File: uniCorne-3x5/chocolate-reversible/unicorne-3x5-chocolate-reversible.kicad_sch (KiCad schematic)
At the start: 87 parts, among them J1 MJ-4PP-9, J2 Conn_01x05, J3 Conn_01x02, J3 Conn_01x03, SW1 SW_CHOC_HS, SW10 SW_CHOC_HS, SW11 SW_CHOC_HS, SW12 SW_CHOC_HS, SW13 SW_CHOC_HS, SW14 SW_CHOC_HS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

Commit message: amended chocolate 3x5
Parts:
- U1: footprint TB2086_MISC:ProMicro-ish-dn-rev-unrouted_3x5 -> TB2086_MISC:ProMicro-ish-dn-rev-unrouted_3x6
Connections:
- net BAT+: now also PSW1.1 (A); no longer PSW1.3 (C)

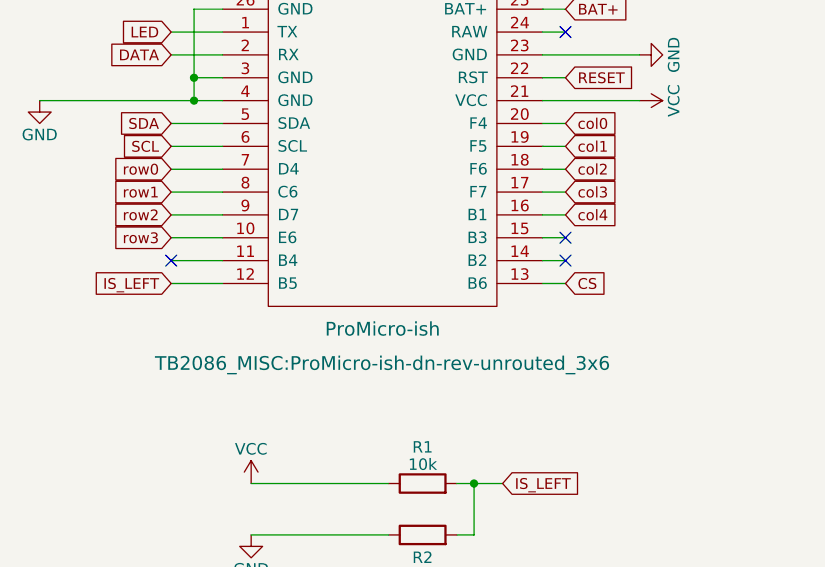
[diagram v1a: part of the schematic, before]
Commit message: fixed footprint for promicro-ish 3x6
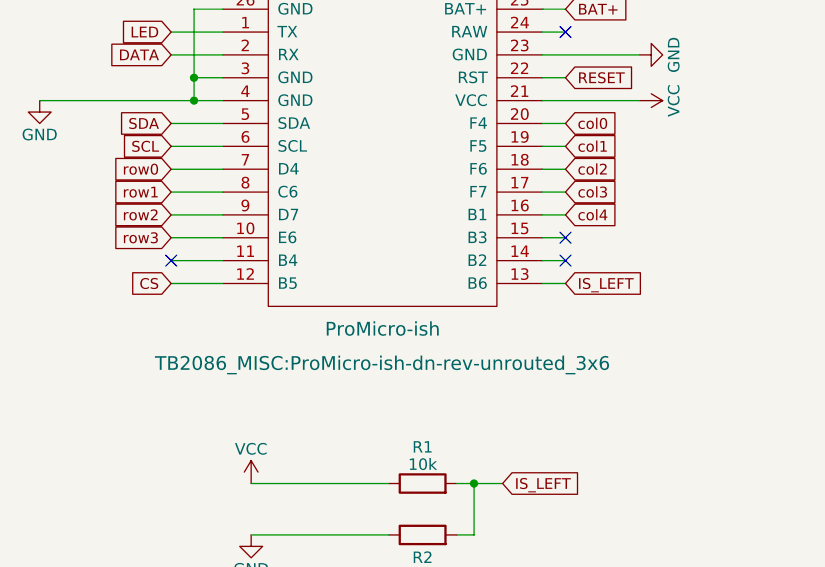
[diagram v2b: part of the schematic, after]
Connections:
- net CS: now also U1.12 (B5); no longer U1.13 (B6)
- net IS_LEFT: now also U1.13 (B6); no longer U1.12 (B5)
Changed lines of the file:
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@@
     )
   )
-  (global_label "CS" (shape input) (at 80.645 54.61 0) (fields_autoplaced)
+  (global_label "IS_LEFT" (shape input) (at 80.645 54.61 0) (fields_autoplaced)
     (effects (font (size 1.1938 1.1938)) (justify left))
-    (property "Intersheetrefs" "${INTERSHEET_REFS}" (at 85.7069 54.61 0)
+    (property "Intersheetrefs" "${INTERSHEET_REFS}" (at 89.9706 54.61 0)
       (effects (font (size 1.27 1.27)) (justify left) hide)
     )
@@
     )
   )
-  (global_label "IS_LEFT" (shape input) (at 36.83 54.61 180) (fields_autoplaced)
+  (global_label "CS" (shape input) (at 36.83 54.61 180) (fields_autoplaced)
     (effects (font (size 1.1938 1.1938)) (justify right))
-    (property "Intersheetrefs" "${INTERSHEET_REFS}" (at 27.5044 54.61 0)
+    (property "Intersheetrefs" "${INTERSHEET_REFS}" (at 31.7681 54.61 0)
       (effects (font (size 1.27 1.27)) (justify right) hide)
     )

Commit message: fixed 3x5
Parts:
- added JP10, JP11: (no value), TB2086_MISC:SolderJumper-2_P1.3mm_Open_TrianglePad1.0x1.2mm_rev, symbol Jumper:Jumper_2_Open
- U1: footprint TB2086_MISC:ProMicro-ish-dn-rev-unrouted_3x6 -> TB2086_MISC:ProMicro-ish-dn-rev-unrouted_3x5
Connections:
- net BAT+: now also U1.24 (RAW)
- net GND: now also JP11.2 (B); no longer U1.26 (GND)
- net SCL: now also JP10.1 (A); no longer J1.A
- new net: J1.A, JP10.2 (B)
- new net B-/D-: JP11.1 (A), U1.26 (B-/D-)
- no-connect marks 6 -> 5
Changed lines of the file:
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@@
   (junction (at 361.95 198.12) (diameter 0) (color 0 0 0 0)
   )
-  (junction (at 39.37 31.75) (diameter 0) (color 0 0 0 0)
-  )
   (junction (at 53.975 129.54) (diameter 0) (color 0 0 0 0)
   )
@@
   )
   (no_connect (at 36.83 52.07))
-  (no_connect (at 80.645 26.67))
   (no_connect (at 261.62 168.91))
   (no_connect (at 59.69 207.645))
@@
     (stroke (width 0) (type default))
   )
-  (wire (pts (xy 108.585 119.38) (xy 156.845 119.38))
+  (wire (pts (xy 108.585 119.38) (xy 117.475 119.38))
     (stroke (width 0) (type default))
   )
@@
     (stroke (width 0) (type default))
   )
-  (wire (pts (xy 39.37 24.13) (xy 39.37 31.75))
-    (stroke (width 0) (type default))
-  )
   (wire (pts (xy 257.81 95.885) (xy 254 95.885))
     (stroke (width 0) (type default))
@@
     (stroke (width 0) (type default))
   )
+  (wire (pts (xy 124.587 171.196) (xy 124.587 168.656))
+    (stroke (width 0) (type default))
+  )
   (wire (pts (xy 36.83 36.83) (xy 42.545 36.83))
     (stroke (width 0) (type default))
@@
     (stroke (width 0) (type default))
   )
-  (wire (pts (xy 42.545 24.13) (xy 39.37 24.13))
+  (wire (pts (xy 42.545 24.13) (xy 36.83 24.13))
     (stroke (width 0) (type default))
   )
@@
     (stroke (width 0) (type default))
   )
+  (wire (pts (xy 127.635 119.38) (xy 156.845 119.38))
+    (stroke (width 0) (type default))
+  )
   (wire (pts (xy 396.24 246.38) (xy 370.84 246.38))
     (stroke (width 0) (type default))
@@
     (stroke (width 0) (type default))
   )
+  (wire (pts (xy 146.304 168.656) (xy 153.797 168.656))
+    (stroke (width 0) (type default))
+  )
   (wire (pts (xy 168.91 123.19) (xy 168.91 119.38))
     (stroke (width 0) (type default))
@@
   )
   (wire (pts (xy 370.84 224.79) (xy 370.84 228.6))
+    (stroke (width 0) (type default))
+  )
+  (wire (pts (xy 124.587 168.656) (xy 136.144 168.656))
     (stroke (width 0) (type default))
   )
@@
   (global_label "BAT+" (shape input) (at 80.645 24.13 0) (fields_autoplaced)
     (effects (font (size 1.1938 1.1938)) (justify left))
-    (property "Intersheetrefs" "${INTERSHEET_REFS}" (at 87.9808 24.13 0)
+    (property "Intersheetrefs" "${INTERSHEET_REFS}" (at 88.0554 24.13 0)
       (effects (font (size 1.27 1.27)) (justify left) hide)
     )
@@
     )
   )
+  (global_label "B-{slash}D-" (shape input) (at 153.797 168.656 0) (fields_autoplaced)
+    (effects (font (size 1.1938 1.1938)) (justify left))
+    (property "Intersheetrefs" "${INTERSHEET_REFS}" (at 163.1969 168.656 0)
+      (effects (font (size 1.27 1.27)) (justify left) hide)
+    )
+  )
   (global_label "col1" (shape input) (at 80.645 39.37 0) (fields_autoplaced)
     (effects (font (size 1.1938 1.1938)) (justify left))
@@
     (effects (font (size 1.524 1.524)) (justify left))
     (property "Intersheetrefs" "${INTERSHEET_REFS}" (at 81.2781 145.415 0)
+      (effects (font (size 1.27 1.27)) (justify left) hide)
+    )
+  )
+  (global_label "BAT+" (shape input) (at 80.645 26.67 0) (fields_autoplaced)
+    (effects (font (size 1.1938 1.1938)) (justify left))
+    (property "Intersheetrefs" "${INTERSHEET_REFS}" (at 88.0554 26.67 0)
       (effects (font (size 1.27 1.27)) (justify left) hide)
     )
@@
     )
   )
+  (global_label "B-{slash}D-" (shape input) (at 36.83 24.13 180) (fields_autoplaced)
+    (effects (font (size 1.1938 1.1938)) (justify right))
+    (property "Intersheetrefs" "${INTERSHEET_REFS}" (at 27.4301 24.13 0)
+      (effects (font (size 1.27 1.27)) (justify right) hide)
+    )
+  )
   (global_label "col2" (shape input) (at 80.645 41.91 0) (fields_autoplaced)
     (effects (font (size 1.1938 1.1938)) (justify left))
@@
     )
   )
+  (symbol (lib_id "Jumper:Jumper_2_Open") (at 141.224 168.656 0) (mirror y) (unit 1)
+    (in_bom yes) (on_board yes) (dnp no)
+    (property "Reference" "JP11" (at 141.224 166.624 0)
+      (effects (font (size 1.27 1.27)))
+    )
+    (property "Value" " " (at 140.97 170.18 0)
+      (effects (font (size 1.27 1.27)))
+    )
+    (property "Footprint" "TB2086_MISC:SolderJumper-2_P1.3mm_Open_TrianglePad1.0x1.2mm_rev" (at 141.224 168.656 0)
+      (effects (font (size 1.27 1.27)) hide)
+    )
+    (property "Datasheet" "~" (at 141.224 168.656 0)
+      (effects (font (size 1.27 1.27)) hide)
+    )
+    (pin "1")
+    (pin "2")
+    (instances
+      (project "unicorne-3x5-chocolate-reversible"
+        (path "/ea5c1f8d-7557-4cbf-a5a2-ee0a51c138e9"
+          (reference "JP11") (unit 1)
+        )
+      )
+    )
+  )
   (symbol (lib_id "Jumper:Jumper_2_Open") (at 64.77 133.985 180) (unit 1)
     (in_bom yes) (on_board yes) (dnp no)
@@
   (symbol (lib_id "TB2086_SMD:SMT 2X4X3.5MM Tactile Tact Push Button") (at 94.615 93.98 0) (unit 1)
     (in_bom yes) (on_board yes) (dnp no) (fields_autoplaced)
-    (property "Reference" "RSW1" (at 94.615 88.8111 0)
-      (effects (font (size 1.27 1.27)))
-    )
-    (property "Value" "SMT 2X4X3.5MM Tactile Tact Push Button" (at 94.615 96.012 0)
+    (property "Reference" "RSW1" (at 94.615 86.36 0)
+      (effects (font (size 1.27 1.27)))
+    )
+    (property "Value" "SMT 2X4X3.5MM Tactile Tact Push Button" (at 94.615 88.9 0)
       (effects (font (size 1.27 1.27)))
     )
     (property "Footprint" "TB2086_SMD:SMT 2X4X3.5MM Tactile Tact Push Button rev" (at 94.6404 99.314 0)
-      (effects (font (size 1.27 1.27)))
+      (effects (font (size 1.27 1.27)) hide)
     )
     (property "Datasheet" "" (at 94.615 93.98 0)
@@
     )
   )
+  (symbol (lib_id "Jumper:Jumper_2_Open") (at 122.555 119.38 0) (mirror y) (unit 1)
+    (in_bom yes) (on_board yes) (dnp no)
+    (property "Reference" "JP10" (at 122.555 117.348 0)
+      (effects (font (size 1.27 1.27)))
+    )
+    (property "Value" " " (at 122.301 120.904 0)
+      (effects (font (size 1.27 1.27)))
+    )
+    (property "Footprint" "TB2086_MISC:SolderJumper-2_P1.3mm_Open_TrianglePad1.0x1.2mm_rev" (at 122.555 119.38 0)
+      (effects (font (size 1.27 1.27)) hide)
+    )
+    (property "Datasheet" "~" (at 122.555 119.38 0)
+      (effects (font (size 1.27 1.27)) hide)
+    )
+    (pin "1")
+    (pin "2")
+    (instances
+      (project "unicorne-3x5-chocolate-reversible"
+        (path "/ea5c1f8d-7557-4cbf-a5a2-ee0a51c138e9"
+          (reference "JP10") (unit 1)
+        )
+      )
+    )
+  )
   (symbol (lib_id "power:PWR_FLAG") (at 400.05 20.32 180) (unit 1)
     (in_bom yes) (on_board yes) (dnp no)
@@
       (effects (font (size 1.524 1.524)))
     )
-    (property "Footprint" "TB2086_MISC:ProMicro-ish-dn-rev-unrouted_3x6" (at 60.325 63.5 0)
-      (effects (font (size 1.524 1.524)))
+    (property "Footprint" "TB2086_MISC:ProMicro-ish-dn-rev-unrouted_3x5" (at 62.865 72.39 0)
+      (effects (font (size 1.524 1.524)) hide)
     )
     (property "Datasheet" "" (at 62.865 72.39 0)
@@
         )
       )
+    )
+  )
+  (symbol (lib_id "power:GND") (at 124.587 171.196 0) (mirror y) (unit 1)
+    (in_bom yes) (on_board yes) (dnp no)
+    (property "Reference" "#PWR010" (at 124.587 177.546 0)
+      (effects (font (size 1.27 1.27)) hide)
+    )
+    (property "Value" "GND" (at 124.714 175.133 0)
+      (effects (font (size 1.27 1.27)))
+    )
+    (property "Footprint" "" (at 124.587 171.196 0)
+      (effects (font (size 1.27 1.27)) hide)
+    )
+    (property "Datasheet" "" (at 124.587 171.196 0)
+      (effects (font (size 1.27 1.27)) hide)
+    )
+    (pin "1")
+    (instances
+      (project "unicorne-3x5-chocolate-reversible"
+        (path "/ea5c1f8d-7557-4cbf-a5a2-ee0a51c138e9"
+          (reference "#PWR010") (unit 1)
+        )
+      )

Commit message: KiCAD 8
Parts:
- JP10, JP11: value (none) -> (none)
